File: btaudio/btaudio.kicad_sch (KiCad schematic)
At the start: 55 parts, among them J1 BAT_CON, J2 USB_C_Receptacle_USB2.0_16P, SW1 POWER_SW, SW2 PLAY/VOL+, SW3 PAUSE/VOL-, SW4 PREV/BT PAIRING, SW5 NEXT/BT DISCONNECT, SW6 SOFT RESET, U1 EWM104-BT5125, U2 PCM5102AQPWRQ1, U3 TPA6132A2RTET, U5 MCP1700x-330xxTT

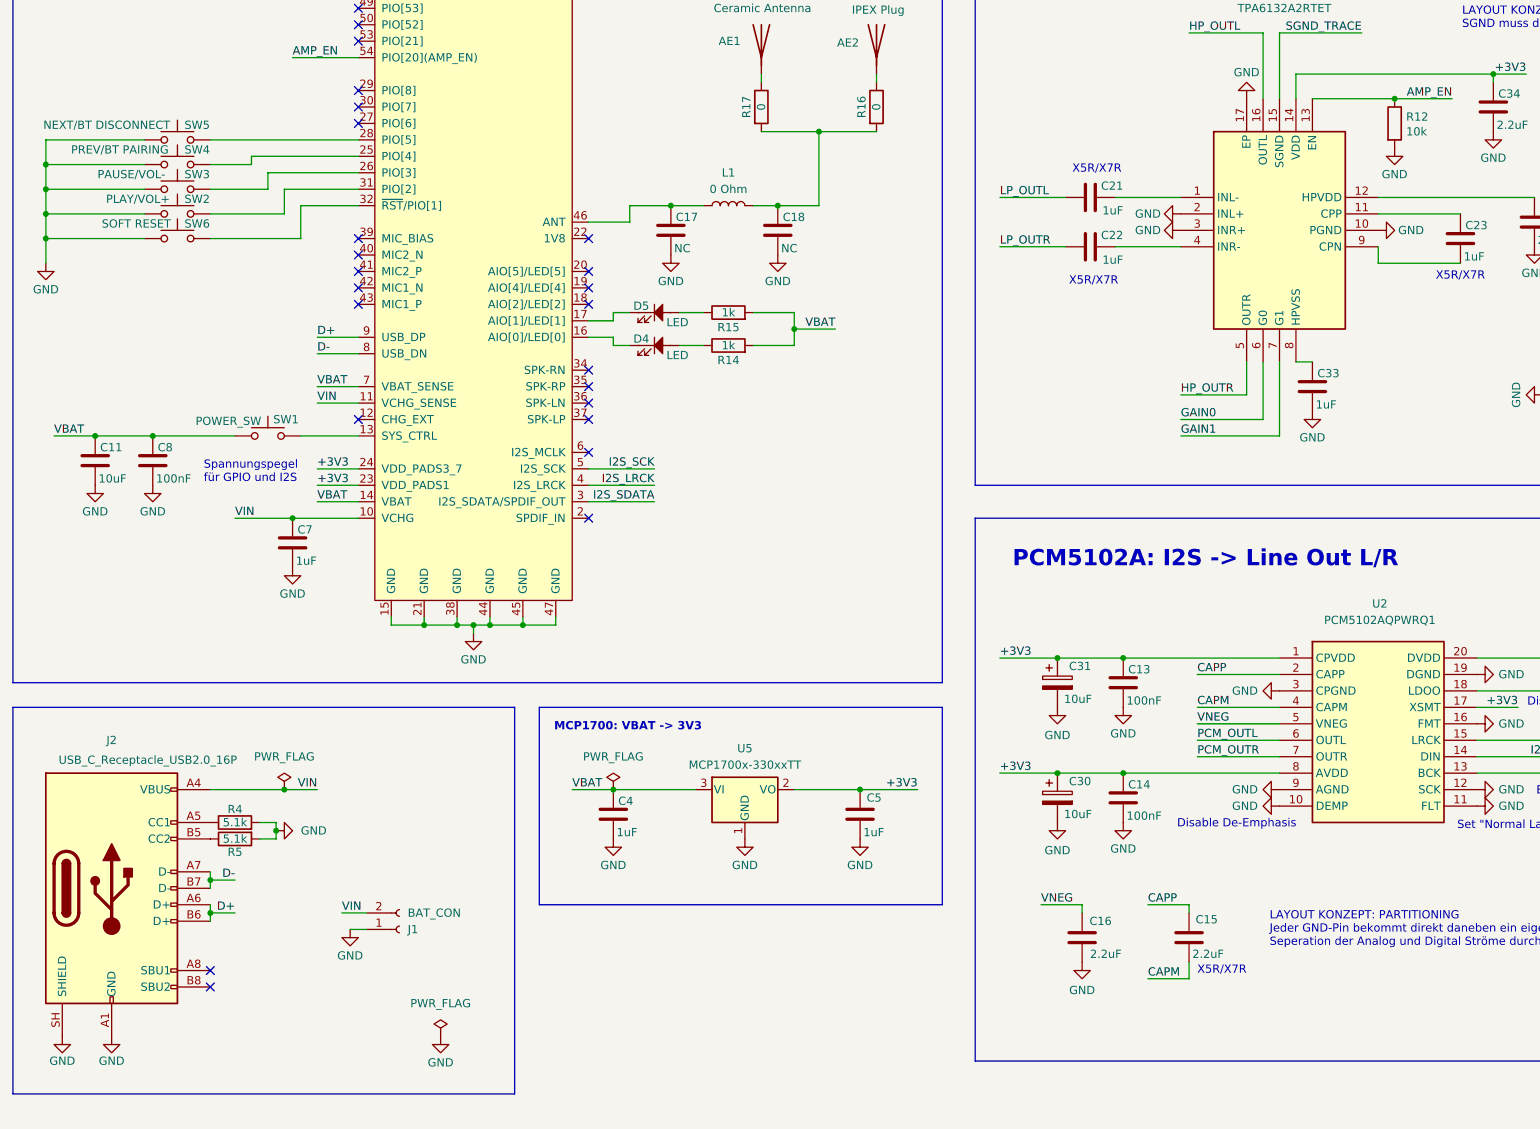
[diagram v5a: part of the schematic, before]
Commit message: footprints assigned, img added
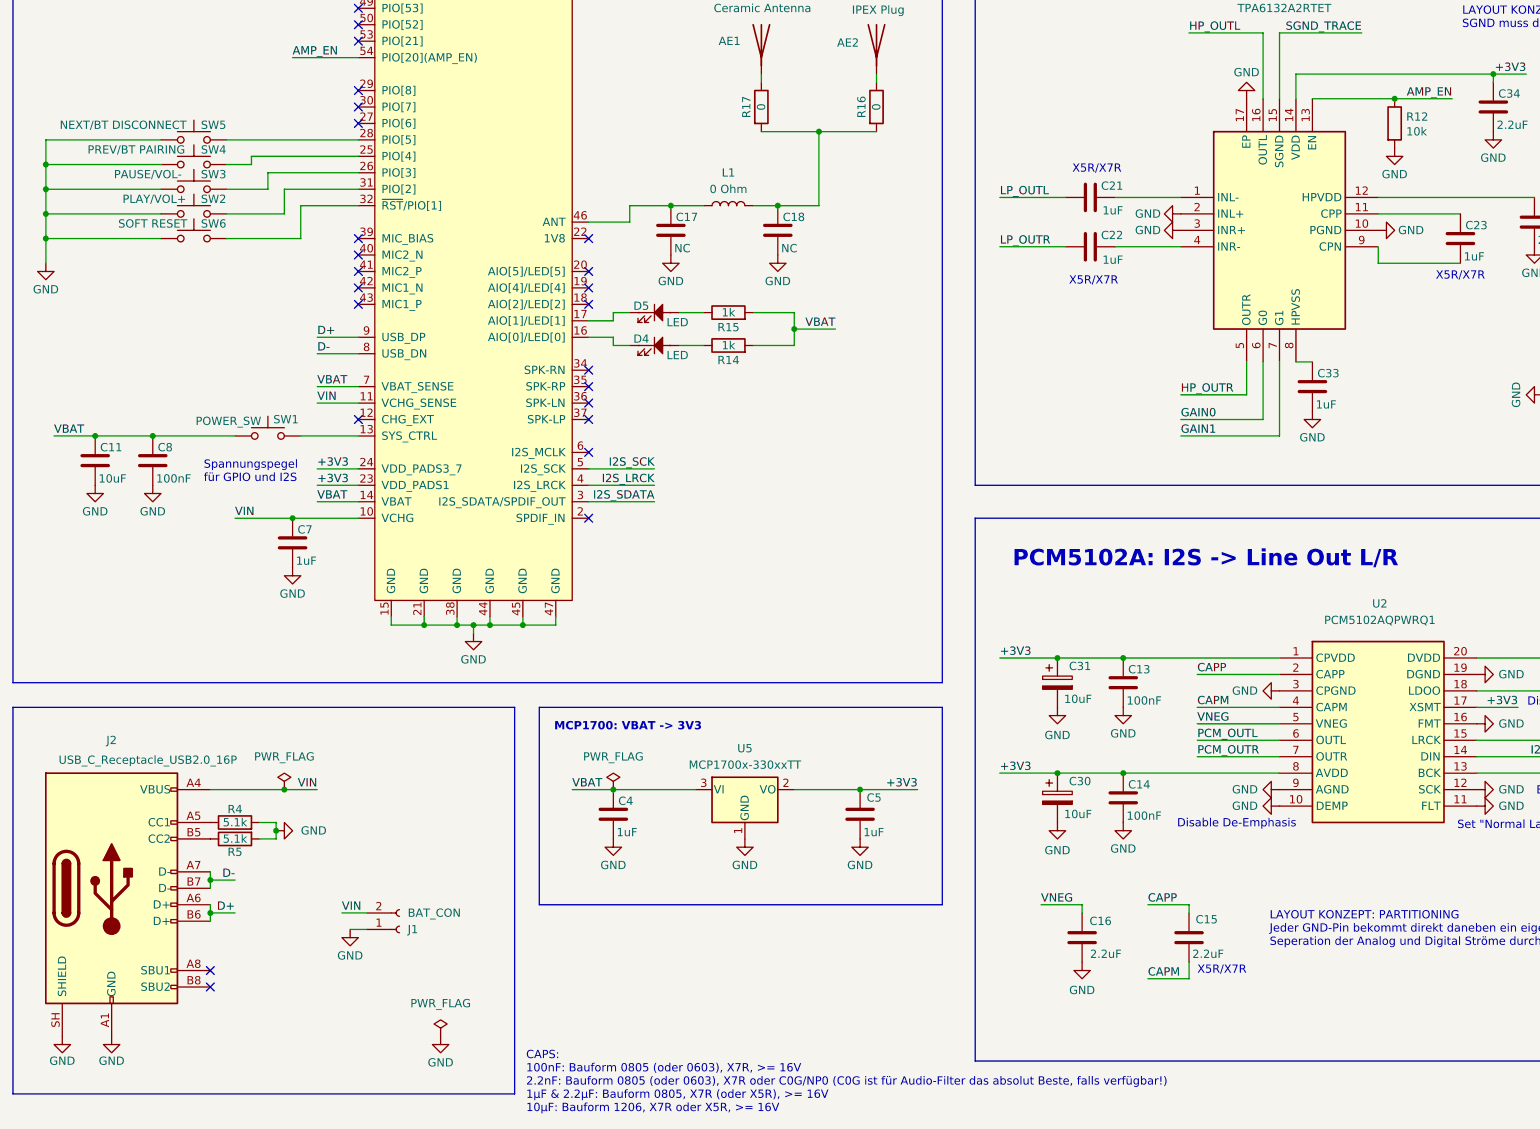
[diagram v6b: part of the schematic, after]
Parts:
- AE1: footprint (none) -> 2450AT18A0100001E:2450AT18A0100001E
- AE2: footprint (none) -> A-1JB:A1JB
- C11, C25, C27, C30, C31: footprint (none) -> Capacitor_SMD:C_1206_3216Metric_Pad1.33x1.80mm_HandSolder
- C13, C14, C15, C16, C21, C22, C23, C24, C26, C28, C29, C32, C33, C34, C4, C5, C7, C8: footprint (none) -> Capacitor_SMD:C_0805_2012Metric_Pad1.18x1.45mm_HandSolder
- C17, C18: footprint (none) -> Capacitor_SMD:C_01005_0402Metric
- JP2: footprint (none) -> Jumper:SolderJumper-3_P1.3mm_Open_RoundedPad1.0x1.5mm
- J_HP1: footprint (none) -> Connector_Audio:Jack_3.5mm_PJ320E_Horizontal
- L1: footprint (none) -> Inductor_SMD:L_0402_1005Metric
- R10, R11, R12, R14, R15, R4, R5: footprint (none) -> Resistor_SMD:R_0805_2012Metric_Pad1.20x1.40mm_HandSolder
- R16, R17: footprint (none) -> Resistor_SMD:R_0402_1005Metric
- SW1, SW2, SW3, SW4, SW5, SW6: footprint (none) -> Button_Switch_SMD:SW_SPST_TS-1088-xR020
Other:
- note added: "CAPS: 100nF: Bauform 0805 (oder 0603), X7R, >= 16V 2.2nF: Bauform 0805 (oder 0603), X7R oder C0G/NP0 (C0G ist für Audio-Filter das absolut Beste, falls verfügbar!) 1μF & 2.2μF: Bauform 0805, X7R (oder X5R), >= 16V 10μF: Bauform 1206, X7R oder X5R, >= 16V"
- moved on the sheet: SW2, SW3, SW4, SW5, SW6

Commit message: bom & fix footprint
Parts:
- C17, C18: footprint Capacitor_SMD:C_01005_0402Metric -> Capacitor_SMD:C_0402_1005Metric
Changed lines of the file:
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@@
 			)
 		)
-		(property "Footprint" "Capacitor_SMD:C_01005_0402Metric"
+		(property "Footprint" "Capacitor_SMD:C_0402_1005Metric"
 			(at 122.8852 81.28 0)
 			(hide yes)
@@
 			)
 		)
-		(property "Footprint" "Capacitor_SMD:C_01005_0402Metric"
+		(property "Footprint" "Capacitor_SMD:C_0402_1005Metric"
 			(at 139.3952 81.28 0)
 			(hide yes)

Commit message: started on layout
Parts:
- removed AE1: Ceramic Antenna, 2450AT18A0100001E:2450AT18A0100001E, symbol Device:Antenna
- removed J_HP1: AudioJack_3.5mm, Connector_Audio:Jack_3.5mm_PJ320E_Horizontal, symbol AudioJack3
- removed R16, R17: 0, Resistor_SMD:R_0402_1005Metric, symbol Device:R
- added J4: AudioJack4, Connector_Audio:Jack_3.5mm_PJ320E_Horizontal, symbol Connector_Audio:AudioJack4
- D4, D5: footprint LED_THT:LED_D5.0mm -> LED_SMD:LED_0805_2012Metric_Pad1.15x1.40mm_HandSolder
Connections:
- net HP_OUTL: now also J4.T
- net HP_OUTR: now also J4.R1
- net SGND_TRACE: now also J4.R2
- net VBAT: now also J1.2 (Pin_2)
- net VIN: no longer J1.2 (Pin_2)
- net at C18.1, L1.2: now also AE2.1 (A)
- no-connect marks 27 -> 28
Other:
- note added: "Physical PJ-320E Pin KiCad Function 1 S Sleeve (Mic) 2 R2 Ring 2 (GND) 3 R1 Ring 1 (Right) 4 T Tip (Left) 5 SW Switch/NC"
- moved on the sheet: AE2, NT1
